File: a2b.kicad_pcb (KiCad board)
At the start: 2 copper layers, 10 parts, among them J1 RAPC722X, J2 PPPC031LFBN-RC, J3 NMJ6HCD2, J4 PPPC031LFBN-RC, J5 NMJ6HCD2, J6 PPPC031LFBN-RC, SW1 ANT21SECQE, SW2 ANT21SECQE

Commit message: UPDATE PCB
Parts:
- removed the J2 at (135.4, 135.0)
- removed the J4 at (165.0, 135.0)
- added J10: Conn_01x01, TestPoint:TestPoint_THTPad_D2.0mm_Drill1.0mm, F.Cu at (164.7, 114.3)
- added J11: Conn_01x01, TestPoint:TestPoint_THTPad_D2.0mm_Drill1.0mm, F.Cu at (167.3, 114.3)
- added J12: Conn_01x01, TestPoint:TestPoint_THTPad_D2.0mm_Drill1.0mm, F.Cu at (169.8, 114.3)
- added J13: Conn_01x01, TestPoint:TestPoint_THTPad_D2.0mm_Drill1.0mm, F.Cu at (128.2, 114.3)
- added J14: Conn_01x01, TestPoint:TestPoint_THTPad_D2.0mm_Drill1.0mm, F.Cu at (130.7, 114.3)
- added J15: Conn_01x01, TestPoint:TestPoint_THTPad_D2.0mm_Drill1.0mm, F.Cu at (133.2, 114.3)
- added J16: Conn_01x01, TestPoint:TestPoint_THTPad_D2.0mm_Drill1.0mm, F.Cu at (144.8, 127.0)
- added J17: Conn_01x01, TestPoint:TestPoint_THTPad_D2.0mm_Drill1.0mm, F.Cu at (144.8, 129.5)
- added J18: Conn_01x01, TestPoint:TestPoint_THTPad_D2.0mm_Drill1.0mm, F.Cu at (144.8, 132.1)
- added J19: Conn_01x01, TestPoint:TestPoint_THTPad_D2.0mm_Drill1.0mm, F.Cu at (152.4, 127.0)
- added J2: Conn_01x01, TestPoint:TestPoint_THTPad_D2.0mm_Drill1.0mm, F.Cu at (124.5, 129.5)
- added J2: Conn_01x01, TestPoint:TestPoint_Pad_D1.5mm, F.Cu at (1.27, 1.27)
- added J2: Conn_01x01, TestPoint:TestPoint_THTPad_D2.0mm_Drill1.0mm, F.Cu at (124.5, 132.1)
- added J2: Conn_01x01, TestPoint:TestPoint_THTPad_D2.0mm_Drill1.0mm, F.Cu at (170.2, 129.5)
- added J20: Conn_01x01, TestPoint:TestPoint_THTPad_D2.0mm_Drill1.0mm, F.Cu at (152.4, 129.5)
- added J21: Conn_01x01, TestPoint:TestPoint_THTPad_D2.0mm_Drill1.0mm, F.Cu at (152.4, 132.1)
- added J4: Conn_01x01, TestPoint:TestPoint_THTPad_D2.0mm_Drill1.0mm, F.Cu at (127.0, 132.1)
- added J4: Conn_01x01, TestPoint:TestPoint_THTPad_D2.0mm_Drill1.0mm, F.Cu at (127.0, 129.5)
- added J4: Conn_01x01, TestPoint:TestPoint_THTPad_D2.0mm_Drill1.0mm, F.Cu at (172.7, 129.5)
- added J4: Conn_01x01, TestPoint:TestPoint_Pad_D1.5mm, F.Cu at (1.27, 4.83)
- added J7: POS1, TestPoint:TestPoint_THTPad_D2.0mm_Drill1.0mm, F.Cu at (149.9, 116.8)
- added J8: Conn_01x01, TestPoint:TestPoint_THTPad_D2.0mm_Drill1.0mm, F.Cu at (170.2, 132.1)
- added J9: Conn_01x01, TestPoint:TestPoint_THTPad_D2.0mm_Drill1.0mm, F.Cu at (172.7, 132.1)
- added U1: ANT13SECQE, footprints:ANT13SEC_CRS, F.Cu at (153.8, 91.4)
- J6: value PPPC031LFBN-RC -> NEG1; footprint PPPC031LFBN:CONN_PPPC031LFBN-RC_SUL -> TestPoint:TestPoint_THTPad_D2.0mm_Drill1.0mm
- R1: footprint Resistor_THT:R_Bare_Metal_Element_L12.4mm_W4.8mm_P11.40mm -> Resistor_THT:R_Axial_DIN0207_L6.3mm_D2.5mm_P10.16mm_Horizontal
- moved J5 51.5 mm to (158.9, 89.2)
- moved J6 35.3 mm to (147.3, 116.8)
- moved J3 32.6 mm to (122.3, 89.2)
- moved R1 20.5 mm to (153.8, 99.1), turned to -90 degrees
- moved SW1 15.6 mm to (126.0, 106.4), turned to 90 degrees
- moved J1 11.9 mm to (148.7, 76.7)
- moved D1 9.61 mm to (146.2, 104.1), turned to 90 degrees
- moved SW2 4.58 mm to (162.6, 106.4), turned to 90 degrees
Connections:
- J1 pad SLEEVE: Net-(D1-K) -> Net-(J2-Pin_1)
- J3 pad RN: Net-(D1-K) -> Net-(J2-Pin_1)
- J3 pad SN: Net-(D1-K) -> Net-(J2-Pin_1)
- J3 pad TN: Net-(D1-K) -> Net-(J2-Pin_1)
- J5 pad RN: Net-(D1-K) -> Net-(J2-Pin_1)
- J5 pad S: Net-(J5-PadS) -> Net-(J10-Pin_1)
- J5 pad SN: Net-(D1-K) -> Net-(J2-Pin_1)
- J5 pad TN: Net-(D1-K) -> Net-(J2-Pin_1)
- J6 pad 1: Net-(J5-PadS) -> Net-(J2-Pin_1)
- R1 pad 1: Net-(J1-PadPIN) -> Net-(R1-Pad1)
- SW1 pad 1: Net-(J6-Pad3) -> Net-(J13-Pin_1)
- SW1 pad 2: Net-(J5-PadT) -> Net-(J3-PadT)
- SW1 pad 3: Net-(D1-K) -> Net-(J2-Pin_1)
- SW1 pad 4: Net-(J6-Pad2) -> Net-(J14-Pin_1)
- SW1 pad 5: Net-(J5-PadR) -> Net-(J3-PadR)
- SW1 pad 6: Net-(D1-K) -> Net-(J2-Pin_1)
- SW2 pad 1: Net-(J4-Pad3) -> Net-(J2-Pin_1)
- SW2 pad 2: Net-(J3-PadT) -> Net-(J5-PadR)
- SW2 pad 3: Net-(D1-K) -> Net-(J11-Pin_1)
- SW2 pad 4: Net-(J4-Pad2) -> Net-(J2-Pin_1)
- SW2 pad 5: Net-(J3-PadR) -> Net-(J5-PadT)
- SW2 pad 6: Net-(D1-K) -> Net-(J12-Pin_1)
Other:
- board outline added: 58.4 x 68.6 mm

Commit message: ASDF
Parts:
- removed the J2 at (1.27, 1.27)
- removed the J2 at (124.5, 132.1)
- removed the J4 at (127.0, 132.1)
- removed the J4 at (1.27, 4.83)
- removed J8, J9: Conn_01x01, TestPoint:TestPoint_THTPad_D2.0mm_Drill1.0mm
- added REF1: Conn_01x01, TestPoint:TestPoint_THTPad_D2.0mm_Drill1.0mm, F.Cu at (124.5, 132.1)
- added REF2: Conn_01x01, TestPoint:TestPoint_THTPad_D2.0mm_Drill1.0mm, F.Cu at (127.0, 132.1)
- added REF3: Conn_01x01, TestPoint:TestPoint_THTPad_D2.0mm_Drill1.0mm, F.Cu at (170.2, 132.1)
- added REF4: Conn_01x01, TestPoint:TestPoint_THTPad_D2.0mm_Drill1.0mm, F.Cu at (172.7, 132.1)
- renumbered J4 to J1, J2 to J3, J1 to SWITCH

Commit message: update pcb
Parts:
- removed J2, J3, J4, REF1, REF2, REF3, REF4: Conn_01x01, TestPoint:TestPoint_THTPad_D2.0mm_Drill1.0mm
- added B1+1: Conn_01x01, TestPoint:TestPoint_THTPad_D1.5mm_Drill0.7mm, F.Cu at (127.0, 132.1)
- added B1-1: Conn_01x01, TestPoint:TestPoint_THTPad_D1.5mm_Drill0.7mm, F.Cu at (124.5, 132.1)
- added B2+1: Conn_01x01, TestPoint:TestPoint_THTPad_D1.5mm_Drill0.7mm, F.Cu at (172.7, 132.1)
- added B2-1: Conn_01x01, TestPoint:TestPoint_THTPad_D1.5mm_Drill0.7mm, F.Cu at (170.2, 132.1)
- B_R_IN1: renamed from J17; footprint TestPoint:TestPoint_THTPad_D2.0mm_Drill1.0mm -> TestPoint:TestPoint_THTPad_D1.5mm_Drill0.7mm
- B_R_OUT1: renamed from J20; footprint TestPoint:TestPoint_THTPad_D2.0mm_Drill1.0mm -> TestPoint:TestPoint_THTPad_D1.5mm_Drill0.7mm
- B_S_IN1: renamed from J18; footprint TestPoint:TestPoint_THTPad_D2.0mm_Drill1.0mm -> TestPoint:TestPoint_THTPad_D1.5mm_Drill0.7mm
- B_S_OUT1: renamed from J21; footprint TestPoint:TestPoint_THTPad_D2.0mm_Drill1.0mm -> TestPoint:TestPoint_THTPad_D1.5mm_Drill0.7mm
- B_T_IN1: renamed from J16; footprint TestPoint:TestPoint_THTPad_D2.0mm_Drill1.0mm -> TestPoint:TestPoint_THTPad_D1.5mm_Drill0.7mm
- B_T_OUT1: renamed from J19; footprint TestPoint:TestPoint_THTPad_D2.0mm_Drill1.0mm -> TestPoint:TestPoint_THTPad_D1.5mm_Drill0.7mm
- F1+1: renamed from J7; value POS1 -> Conn_01x01; footprint TestPoint:TestPoint_THTPad_D2.0mm_Drill1.0mm -> TestPoint:TestPoint_THTPad_D1.5mm_Drill0.7mm
- F1-1: renamed from J6; value NEG1 -> Conn_01x01; footprint TestPoint:TestPoint_THTPad_D2.0mm_Drill1.0mm -> TestPoint:TestPoint_THTPad_D1.5mm_Drill0.7mm
- J1: value Conn_01x01 -> M20-9990246; footprint TestPoint:TestPoint_THTPad_D2.0mm_Drill1.0mm -> M20-9990246:CONN2_M20-999_1x2_HRW
- R_IN1: renamed from J14; footprint TestPoint:TestPoint_THTPad_D2.0mm_Drill1.0mm -> TestPoint:TestPoint_THTPad_D1.5mm_Drill0.7mm
- R_OUT1: renamed from J11; footprint TestPoint:TestPoint_THTPad_D2.0mm_Drill1.0mm -> TestPoint:TestPoint_THTPad_D1.5mm_Drill0.7mm
- S_IN1: renamed from J15; footprint TestPoint:TestPoint_THTPad_D2.0mm_Drill1.0mm -> TestPoint:TestPoint_THTPad_D1.5mm_Drill0.7mm
- S_OUT1: renamed from J12; footprint TestPoint:TestPoint_THTPad_D2.0mm_Drill1.0mm -> TestPoint:TestPoint_THTPad_D1.5mm_Drill0.7mm
- T_IN1: renamed from J13; footprint TestPoint:TestPoint_THTPad_D2.0mm_Drill1.0mm -> TestPoint:TestPoint_THTPad_D1.5mm_Drill0.7mm
- T_OUT1: renamed from J10; footprint TestPoint:TestPoint_THTPad_D2.0mm_Drill1.0mm -> TestPoint:TestPoint_THTPad_D1.5mm_Drill0.7mm
- moved J1 210.9 mm to (4.39, 2.54)
- moved R_IN1 2.54 mm to (130.7, 116.8)
- moved R_OUT1 2.54 mm to (167.3, 116.8)
- moved S_IN1 2.54 mm to (133.2, 116.8)
- moved S_OUT1 2.54 mm to (169.8, 116.8)
- moved T_IN1 2.54 mm to (128.2, 116.8)
- moved T_OUT1 2.54 mm to (164.7, 116.8)
- renumbered J3 to AUDIO_IN1, SW1 to AUDIO_IN_SW1, J5 to AUDIO_OUT1, SW2 to AUDIO_OUT_SW1, SWITCH to DC_IN1, U1 to POWERSWITCH1
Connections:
- AUDIO_IN1 pad RN: Net-(J2-Pin_1) -> Net-(AUDIO_IN1-PadRN)
- AUDIO_IN1 pad SN: Net-(J2-Pin_1) -> Net-(AUDIO_IN1-PadRN)
- AUDIO_IN1 pad TN: Net-(J2-Pin_1) -> Net-(AUDIO_IN1-PadRN)
- AUDIO_IN_SW1 pad 3: Net-(J2-Pin_1) -> Net-(AUDIO_IN1-PadRN)
- AUDIO_IN_SW1 pad 6: Net-(J2-Pin_1) -> Net-(AUDIO_IN1-PadRN)
- AUDIO_OUT1 pad R: Net-(J5-PadR) -> Net-(AUDIO_OUT1-PadR)
- AUDIO_OUT1 pad RN: Net-(J2-Pin_1) -> Net-(B_S_OUT1-Pin_1)
- AUDIO_OUT1 pad S: Net-(J10-Pin_1) -> Net-(B_S_OUT1-Pin_1)
- AUDIO_OUT1 pad SN: Net-(J2-Pin_1) -> Net-(B_S_OUT1-Pin_1)
- AUDIO_OUT1 pad T: Net-(J5-PadT) -> Net-(AUDIO_OUT1-PadT)
- AUDIO_OUT1 pad TN: Net-(J2-Pin_1) -> Net-(B_S_OUT1-Pin_1)
- AUDIO_OUT_SW1 pad 1: Net-(J2-Pin_1) -> Net-(B_T_OUT1-Pin_1)
- AUDIO_OUT_SW1 pad 2: Net-(J5-PadR) -> Net-(AUDIO_OUT1-PadT)
- AUDIO_OUT_SW1 pad 3: Net-(J11-Pin_1) -> Net-(B_S_OUT1-Pin_1)
- AUDIO_OUT_SW1 pad 4: Net-(J2-Pin_1) -> Net-(B_R_OUT1-Pin_1)
- AUDIO_OUT_SW1 pad 5: Net-(J5-PadT) -> Net-(AUDIO_OUT1-PadR)
- AUDIO_OUT_SW1 pad 6: Net-(J12-Pin_1) -> Net-(B_S_OUT1-Pin_1)
- B_R_OUT1 pad 1: Net-(J11-Pin_1) -> Net-(B_R_OUT1-Pin_1)
- B_S_OUT1 pad 1: Net-(J12-Pin_1) -> Net-(B_S_OUT1-Pin_1)
- B_T_OUT1 pad 1: Net-(J10-Pin_1) -> Net-(B_T_OUT1-Pin_1)
- D1 pad 1: Net-(D1-K) -> Net-(B1+1-Pin_1)
- DC_IN1 pad SLEEVE: Net-(J2-Pin_1) -> Net-(B1-1-Pin_1)
- F1+1 pad 1: Net-(D1-K) -> Net-(B1+1-Pin_1)
- F1-1 pad 1: Net-(J2-Pin_1) -> Net-(B1-1-Pin_1)
- J1 pad 1: Net-(D1-K) -> unconnected-(J1-Pad1)
- R_OUT1 pad 1: Net-(J11-Pin_1) -> Net-(B_R_OUT1-Pin_1)
- S_OUT1 pad 1: Net-(J12-Pin_1) -> Net-(B_S_OUT1-Pin_1)
- T_OUT1 pad 1: Net-(J10-Pin_1) -> Net-(B_T_OUT1-Pin_1)
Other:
- board size 58.4 x 68.6 mm -> 58.4 x 66 mm

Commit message: update pcb and schematic
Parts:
- removed B1+1, B1-1, B2+1, B2-1, F1+1, F1-1: Conn_01x01, TestPoint:TestPoint_THTPad_D1.5mm_Drill0.7mm
- added U1: ~, Connector_PinHeader_2.54mm:PinHeader_1x02_P2.54mm_Vertical, F.Cu at (127.0, 132.1)
- added U2: ~, Connector_PinHeader_2.54mm:PinHeader_1x02_P2.54mm_Vertical, F.Cu at (149.9, 116.8)
- added U3: ~, Connector_PinHeader_2.54mm:PinHeader_1x02_P2.54mm_Vertical, F.Cu at (172.7, 132.1)

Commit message: update pcb
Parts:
- removed B_R_IN1, B_R_OUT1, B_S_IN1, B_S_OUT1, B_T_IN1, B_T_OUT1, R_IN1, R_OUT1, S_IN1, S_OUT1, T_IN1, T_OUT1: Conn_01x01, TestPoint:TestPoint_THTPad_D1.5mm_Drill0.7mm
- added pinout1: ~, Connector_PinHeader_2.54mm:PinHeader_1x03_P2.54mm_Vertical, F.Cu at (132.1, 116.8)
- added pinout2: ~, Connector_PinHeader_2.54mm:PinHeader_1x03_P2.54mm_Vertical, B.Cu at (144.8, 127.0)
- added pinout3: ~, Connector_PinHeader_2.54mm:PinHeader_1x03_P2.54mm_Vertical, B.Cu at (152.4, 127.0)
- added pinout4: ~, Connector_PinHeader_2.54mm:PinHeader_1x03_P2.54mm_Vertical, F.Cu at (170.2, 116.8)
- U1, U3: moved to B.Cu
- turned U1 to 90 degrees
- turned U3 to 90 degrees
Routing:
- net Net-(DC_IN1-PadSLEEVE): track 0.00 -> 122.0 mm
- net Net-(AUDIO_OUT1-PadRN): track 0.00 -> 82.4 mm
- net Net-(D1-K): track 0.00 -> 78.6 mm, vias 0 -> 1
- net Net-(AUDIO_IN1-PadS): track 0.00 -> 62.3 mm
- net Net-(AUDIO_OUT_SW1-Pad4): track 0.00 -> 46.5 mm
- net Net-(AUDIO_IN_SW1-Pad4): track 0.00 -> 39.3 mm
- net Net-(AUDIO_IN_SW1-Pad1): track 0.00 -> 38.2 mm
- net Net-(AUDIO_OUT_SW1-Pad1): track 0.00 -> 33.7 mm
- net Net-(AUDIO_IN1-PadRN): track 0.00 -> 31.3 mm
- net Net-(AUDIO_IN1-PadR): track 0.00 -> 22.3 mm
- net Net-(AUDIO_OUT1-PadR): track 0.00 -> 22.3 mm
- net Net-(AUDIO_IN1-PadT): track 0.00 -> 20.7 mm
- net Net-(AUDIO_OUT1-PadT): track 0.00 -> 20.7 mm
- net Net-(D1-A): track 0.00 -> 10.8 mm
- net Net-(DC_IN1-PadPIN): track 0.00 -> 10.6 mm
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
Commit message: update pcb
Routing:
- net Net-(AUDIO_OUT_SW1-Pad4): track 46.5 -> 49.5 mm

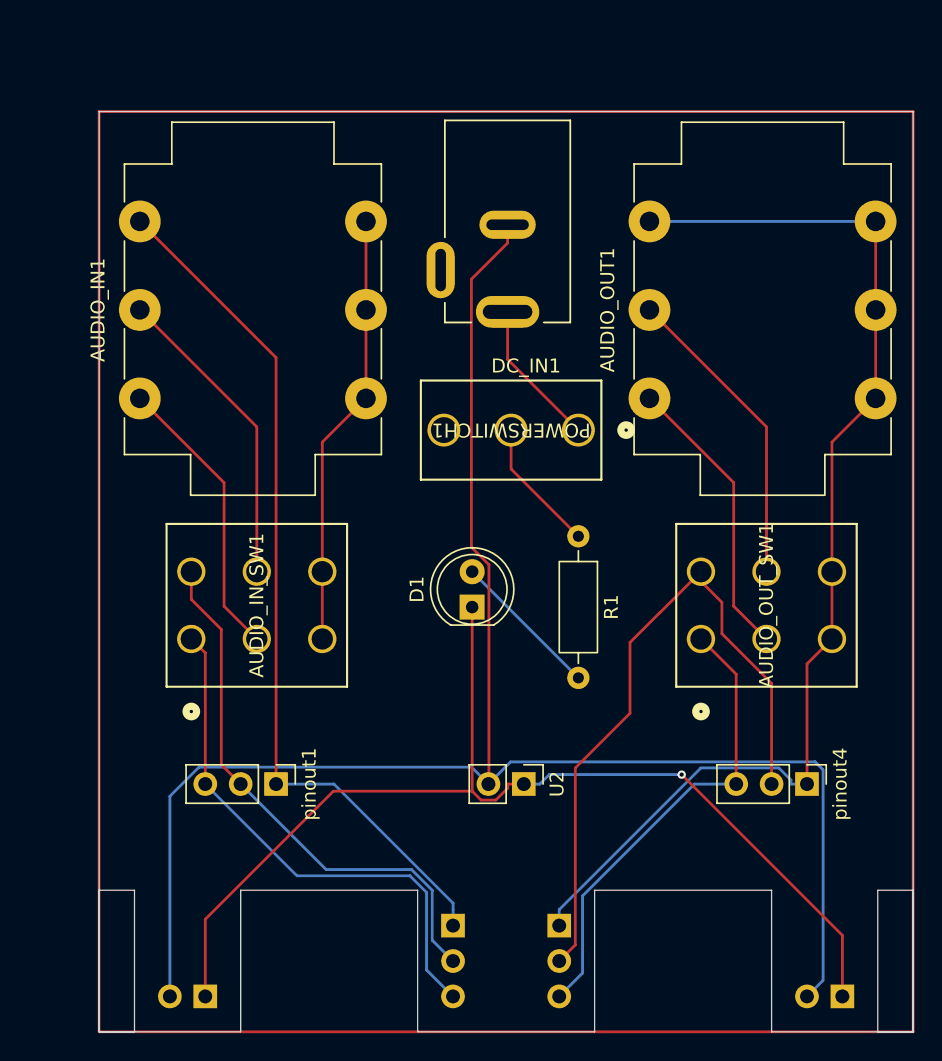
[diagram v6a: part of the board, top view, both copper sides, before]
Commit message: update pcb silkscreens
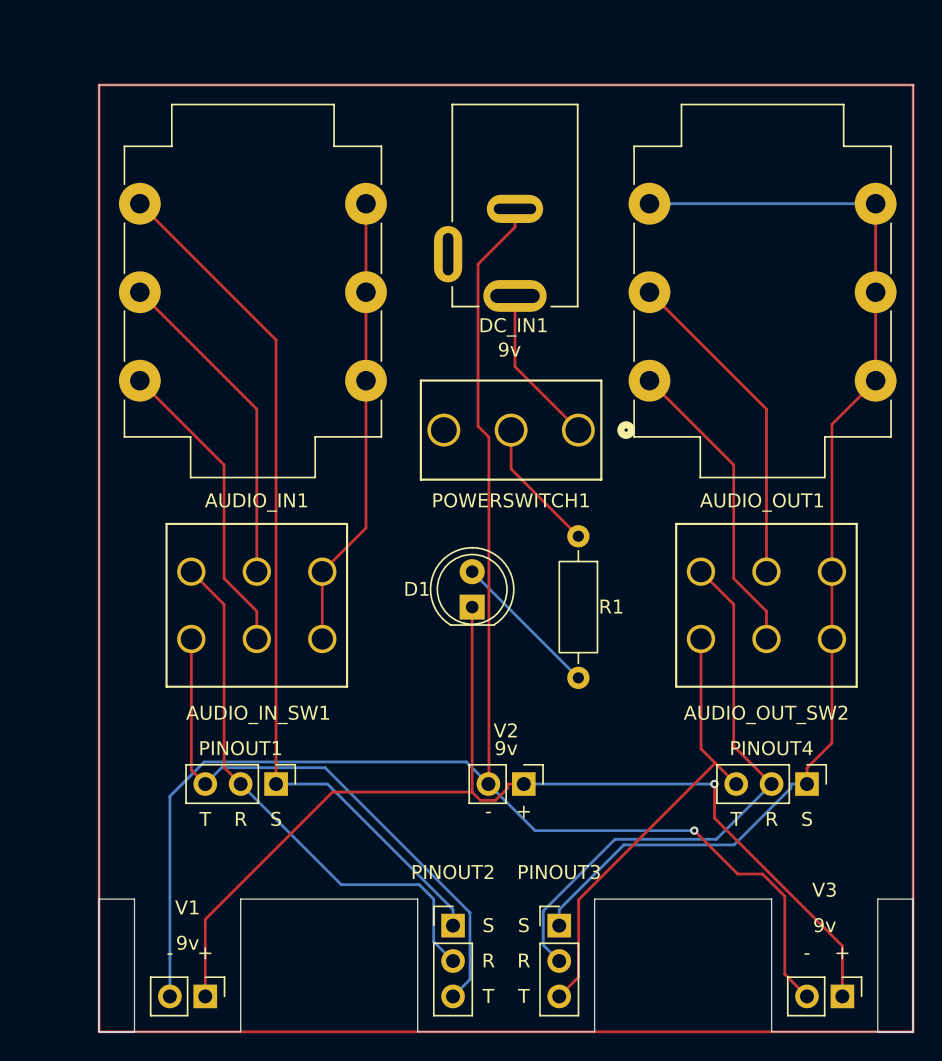
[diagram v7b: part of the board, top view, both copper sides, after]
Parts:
- PINOUT2: renamed from pinout2; moved to F.Cu
- PINOUT3: renamed from pinout3; moved to F.Cu
- V1: renamed from U1; moved to F.Cu
- V3: renamed from U3; moved to F.Cu
- moved AUDIO_IN1 1.27 mm to (122.3, 87.9)
- moved AUDIO_OUT1 1.27 mm to (158.9, 87.9)
- moved DC_IN1 1.26 mm to (149.2, 75.6)
- turned PINOUT2 to 0 degrees
- turned PINOUT3 to 0 degrees
- turned V1 to -90 degrees
- turned V3 to -90 degrees
- renumbered AUDIO_OUT_SW1 to AUDIO_OUT_SW2, pinout1 to PINOUT1, pinout4 to PINOUT4, U2 to V2
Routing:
- net Net-(AUDIO_OUT_SW2-Pad4): track 49.5 -> 41.6 mm
- net Net-(DC_IN1-PadSLEEVE): track 122.0 -> 114.1 mm, vias 0 -> 1
- net Net-(AUDIO_IN_SW1-Pad1): track 38.2 -> 41.1 mm
- net Net-(AUDIO_IN1-PadT): track 20.7 -> 22.0 mm
- net Net-(AUDIO_OUT1-PadT): track 20.7 -> 22.0 mm
- net Net-(AUDIO_IN1-PadRN): track 31.3 -> 32.5 mm
- net Net-(AUDIO_IN1-PadR): track 22.3 -> 23.5 mm
- net Net-(AUDIO_OUT1-PadR): track 22.3 -> 23.5 mm
- net Net-(AUDIO_IN1-PadS): track 62.3 -> 63.3 mm
- net Net-(DC_IN1-PadPIN): track 10.6 -> 11.5 mm
- net Net-(AUDIO_OUT_SW2-Pad1): track 33.7 -> 32.8 mm
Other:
- board size 58.4 x 66 mm -> 58.4 x 67.9 mm
- board text added: "+"
- board text added: "-"
- board text added: "9v"
- board text added: "R"
- board text added: "S"
- board text added: "T"

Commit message: update pcb
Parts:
- PINOUT2, PINOUT3, V1, V3: moved to B.Cu
- turned PINOUT2 to 180 degrees
- turned PINOUT3 to 180 degrees
- turned V1 to 90 degrees
- turned V3 to 90 degrees
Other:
- outline, holes or cut-outs redrawn
